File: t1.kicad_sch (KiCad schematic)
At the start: 47 parts, among them J1 Barrel_Jack_Switch, J2 USB_B, J3 P1, J4 2x2M, J5 ICSP1, J6 P2, U1 ATmega8U2-AU, Y1 16MHz

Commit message: Fixed ERC issues
- Connector names changed from Male to Pin (OMG!)
- Updated power components from KiCad 8 lib
- Synzed the PCB
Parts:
- J3: symbol Connector:Conn_01x05_Male -> Connector:Conn_01x05_Pin
- J6: symbol Connector:Conn_01x06_Male -> Connector:Conn_01x06_Pin

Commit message: Renamed MFN -> MNF and MFP -> MPN
KiCost compatibility
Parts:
- C1: MFN Vishay Beyschlag/Draloric/BC Components -> (none); MFP MAL215371479E3 -> (none); MNF (none) -> Vishay Beyschlag/Draloric/BC Components; MPN (none) -> MAL215371479E3
- D2, D3: MFN OSRAM Opto Semiconductors Inc. -> (none); MFP LG R971-KN-1 -> (none); MNF (none) -> OSRAM Opto Semiconductors Inc.; MPN (none) -> LG R971-KN-1
- FB1: MFN Murata -> (none); MFP BLM21PG221SN1D -> (none); MNF (none) -> Murata; MPN (none) -> BLM21PG221SN1D
- J1: MFN Würth Elektronik -> (none); MFP 694106106102 -> (none); MNF (none) -> Würth Elektronik; MPN (none) -> 694106106102
- J2: MFN TE Connectivity AMP Connectors -> (none); MFP 292304-1 -> (none); MNF (none) -> TE Connectivity AMP Connectors; MPN (none) -> 292304-1
- J4: MFN Harwin Inc. -> (none); MFP M20-9980246-ND -> (none); MNF (none) -> Harwin Inc.; MPN (none) -> M20-9980246-ND
- J5: MFN Harwin Inc. -> (none); MFP M20-9980346 -> (none); MNF (none) -> Harwin Inc.; MPN (none) -> M20-9980346
- VR1, VR2: MFN Bourns Inc. -> (none); MFP CG0603MLC-05E -> (none); MNF (none) -> Bourns Inc.; MPN (none) -> CG0603MLC-05E
- Y1: MFN Abracon LLC -> (none); MFP ABM3-16.000MHZ-B2-T -> (none); MNF (none) -> Abracon LLC; MPN (none) -> ABM3-16.000MHZ-B2-T
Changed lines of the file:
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@@
 			)
 		)
-		(property "MFN" "Bourns Inc."
+		(property "MNF" "Bourns Inc."
 			(at 100.33 119.38 0)
 			(effects
@@
 			)
 		)
-		(property "MFP" "CG0603MLC-05E"
+		(property "MPN" "CG0603MLC-05E"
 			(at 100.33 119.38 0)
 			(effects
@@
 			)
 		)
-		(property "MFN" "Abracon LLC"
+		(property "MNF" "Abracon LLC"
 			(at 120.65 80.01 90)
 			(effects
@@
 			)
 		)
-		(property "MFP" "ABM3-16.000MHZ-B2-T"
+		(property "MPN" "ABM3-16.000MHZ-B2-T"
 			(at 120.65 80.01 90)
 			(effects
@@
 			)
 		)
-		(property "MFN" "TE Connectivity AMP Connectors"
+		(property "MNF" "TE Connectivity AMP Connectors"
 			(at 72.39 107.95 0)
 			(effects
@@
 			)
 		)
-		(property "MFP" "292304-1"
+		(property "MPN" "292304-1"
 			(at 72.39 107.95 0)
 			(effects
@@
 			)
 		)
-		(property "MFN" "Bourns Inc."
+		(property "MNF" "Bourns Inc."
 			(at 91.44 119.38 0)
 			(effects
@@
 			)
 		)
-		(property "MFP" "CG0603MLC-05E"
+		(property "MPN" "CG0603MLC-05E"
 			(at 91.44 119.38 0)
 			(effects
@@
 			)
 		)
-		(property "MFN" "Murata"
+		(property "MNF" "Murata"
 			(at 96.52 130.81 0)
 			(effects
@@
 			)
 		)
-		(property "MFP" "BLM21PG221SN1D"
+		(property "MPN" "BLM21PG221SN1D"
 			(at 96.52 130.81 0)
 			(effects
@@
 			)
 		)
-		(property "MFN" "OSRAM Opto Semiconductors Inc."
+		(property "MNF" "OSRAM Opto Semiconductors Inc."
 			(at 248.92 115.57 90)
 			(effects
@@
 			)
 		)
-		(property "MFP" "LG R971-KN-1"
+		(property "MPN" "LG R971-KN-1"
 			(at 248.92 115.57 90)
 			(effects
@@
 			)
 		)
-		(property "MFN" "Würth Elektronik"
+		(property "MNF" "Würth Elektronik"
 			(at 54.61 50.8 0)
 			(effects
@@
 			)
 		)
-		(property "MFP" "694106106102"
+		(property "MPN" "694106106102"
 			(at 54.61 50.8 0)
 			(effects
@@
 			)
 		)
-		(property "MFN" "Harwin Inc."
+		(property "MNF" "Harwin Inc."
 			(at 213.36 74.93 0)
 			(effects
@@
 			)
 		)
-		(property "MFP" "M20-9980346"
+		(property "MPN" "M20-9980346"
 			(at 213.36 74.93 0)
 			(effects
@@
 			)
 		)
-		(property "MFN" "Harwin Inc."
+		(property "MNF" "Harwin Inc."
 			(at 208.28 86.36 0)
 			(effects
@@
 			)
 		)
-		(property "MFP" "M20-9980246-ND"
+		(property "MPN" "M20-9980246-ND"
 			(at 208.28 86.36 0)
 			(effects
@@
 			)
 		)
-		(property "MFN" "OSRAM Opto Semiconductors Inc."
+		(property "MNF" "OSRAM Opto Semiconductors Inc."
 			(at 236.22 115.57 90)
 			(effects
@@
 			)
 		)
-		(property "MFP" "LG R971-KN-1"
+		(property "MPN" "LG R971-KN-1"
 			(at 236.22 115.57 90)
 			(effects
@@
 			)
 		)
-		(property "MFN" "Vishay Beyschlag/Draloric/BC Components"
+		(property "MNF" "Vishay Beyschlag/Draloric/BC Components"
 			(at 82.55 53.34 0)
 			(effects
@@
 			)
 		)
-		(property "MFP" "MAL215371479E3"
+		(property "MPN" "MAL215371479E3"
 			(at 82.55 53.34 0)
 			(effects

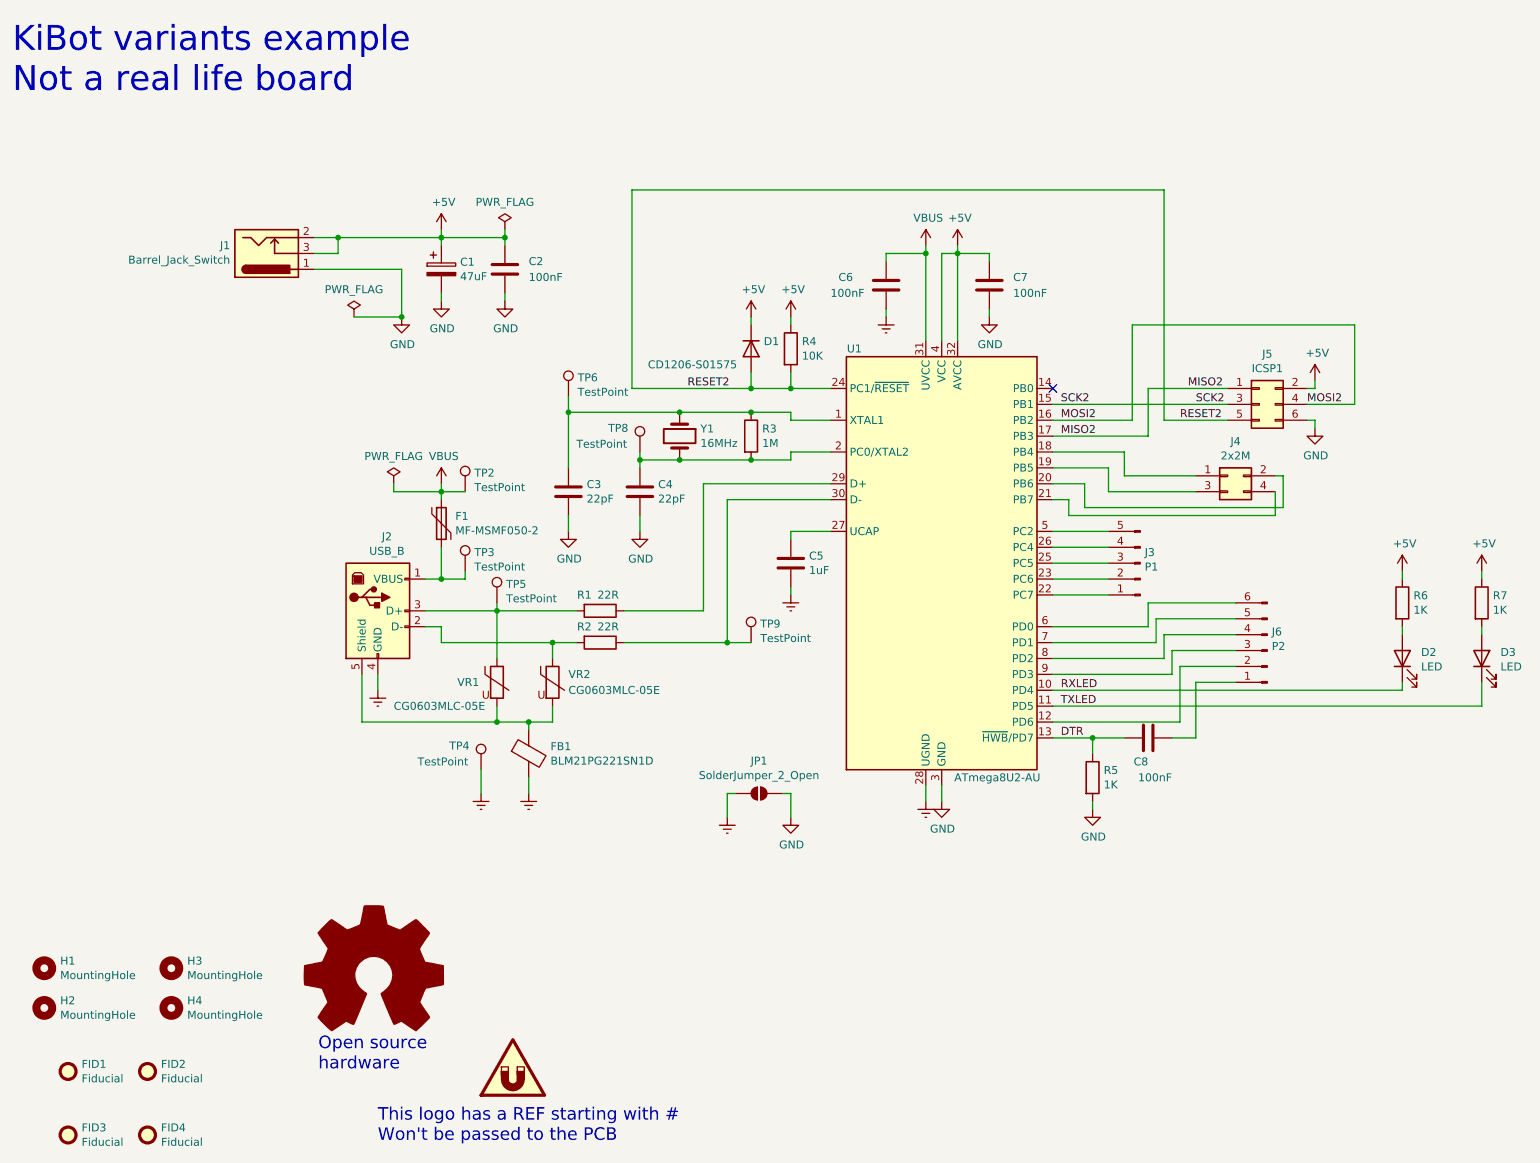
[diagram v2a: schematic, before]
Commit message: Migrated to KiCad 9 for tests
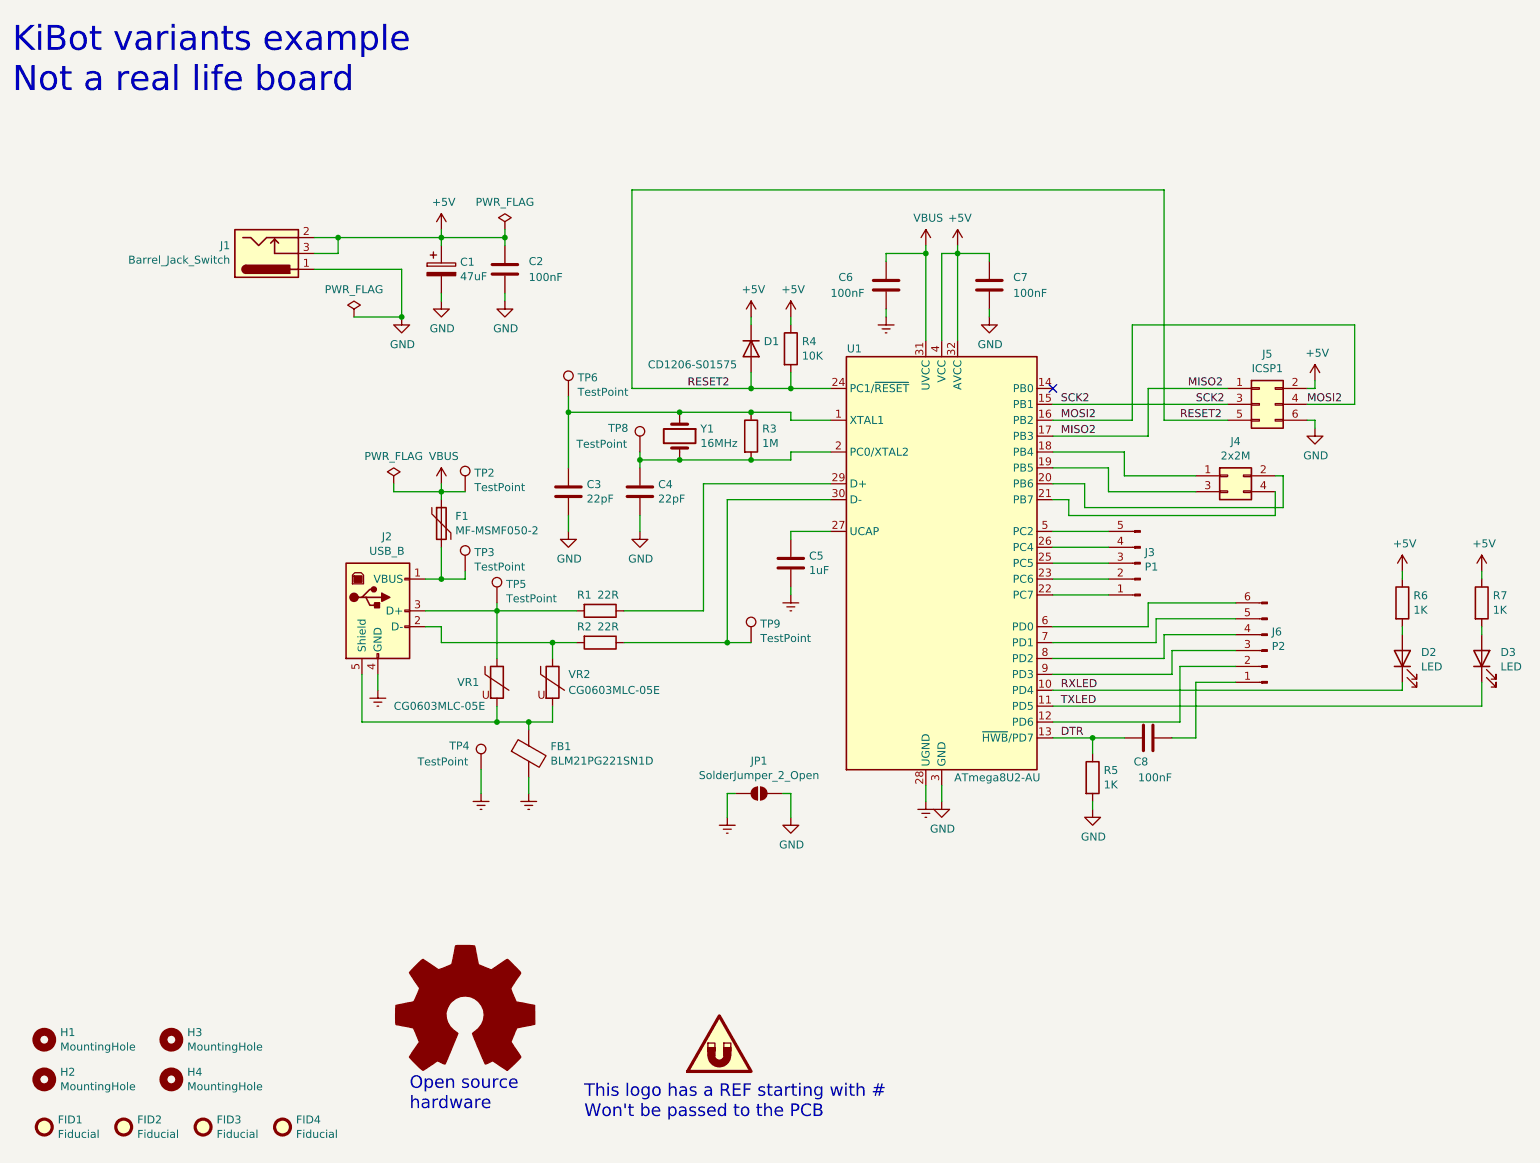
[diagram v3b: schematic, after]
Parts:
- C1: MFN (none) -> Vishay Beyschlag/Draloric/BC Components; MFP (none) -> MAL215371479E3; MNF Vishay Beyschlag/Draloric/BC Components -> (none); MPN MAL215371479E3 -> (none)
- D2, D3: MFN (none) -> OSRAM Opto Semiconductors Inc.; MFP (none) -> LG R971-KN-1; MNF OSRAM Opto Semiconductors Inc. -> (none); MPN LG R971-KN-1 -> (none)
- FB1: MFN (none) -> Murata; MFP (none) -> BLM21PG221SN1D; MNF Murata -> (none); MPN BLM21PG221SN1D -> (none)
- J1: MFN (none) -> Würth Elektronik; MFP (none) -> 694106106102; MNF Würth Elektronik -> (none); MPN 694106106102 -> (none)
- J2: MFN (none) -> TE Connectivity AMP Connectors; MFP (none) -> 292304-1; MNF TE Connectivity AMP Connectors -> (none); MPN 292304-1 -> (none)
- J4: MFN (none) -> Harwin Inc.; MFP (none) -> M20-9980246-ND; MNF Harwin Inc. -> (none); MPN M20-9980246-ND -> (none)
- J5: MFN (none) -> Harwin Inc.; MFP (none) -> M20-9980346; MNF Harwin Inc. -> (none); MPN M20-9980346 -> (none)
- VR1, VR2: MFN (none) -> Bourns Inc.; MFP (none) -> CG0603MLC-05E; MNF Bourns Inc. -> (none); MPN CG0603MLC-05E -> (none)
- Y1: MFN (none) -> Abracon LLC; MFP (none) -> ABM3-16.000MHZ-B2-T; MNF Abracon LLC -> (none); MPN ABM3-16.000MHZ-B2-T -> (none)
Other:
- company: Instituto Nacional de Tecnología Industrial -> Arduino
- moved on the sheet: FID1, FID2, FID3, FID4, H1, H2, H3, H4
